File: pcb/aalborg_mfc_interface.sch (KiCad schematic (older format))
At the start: 27 parts, among them J1 DB15FV, J2 DB15FV, J3 DB15FV, P1 PWR_JACK_2.5x5.5, P2 HEADER_01X03, P3 HEADER_01X03, P4 HEADER_01X03, P5 HEADER_01X03, SW1 SPST_SERIES_M, U1 MAX6817

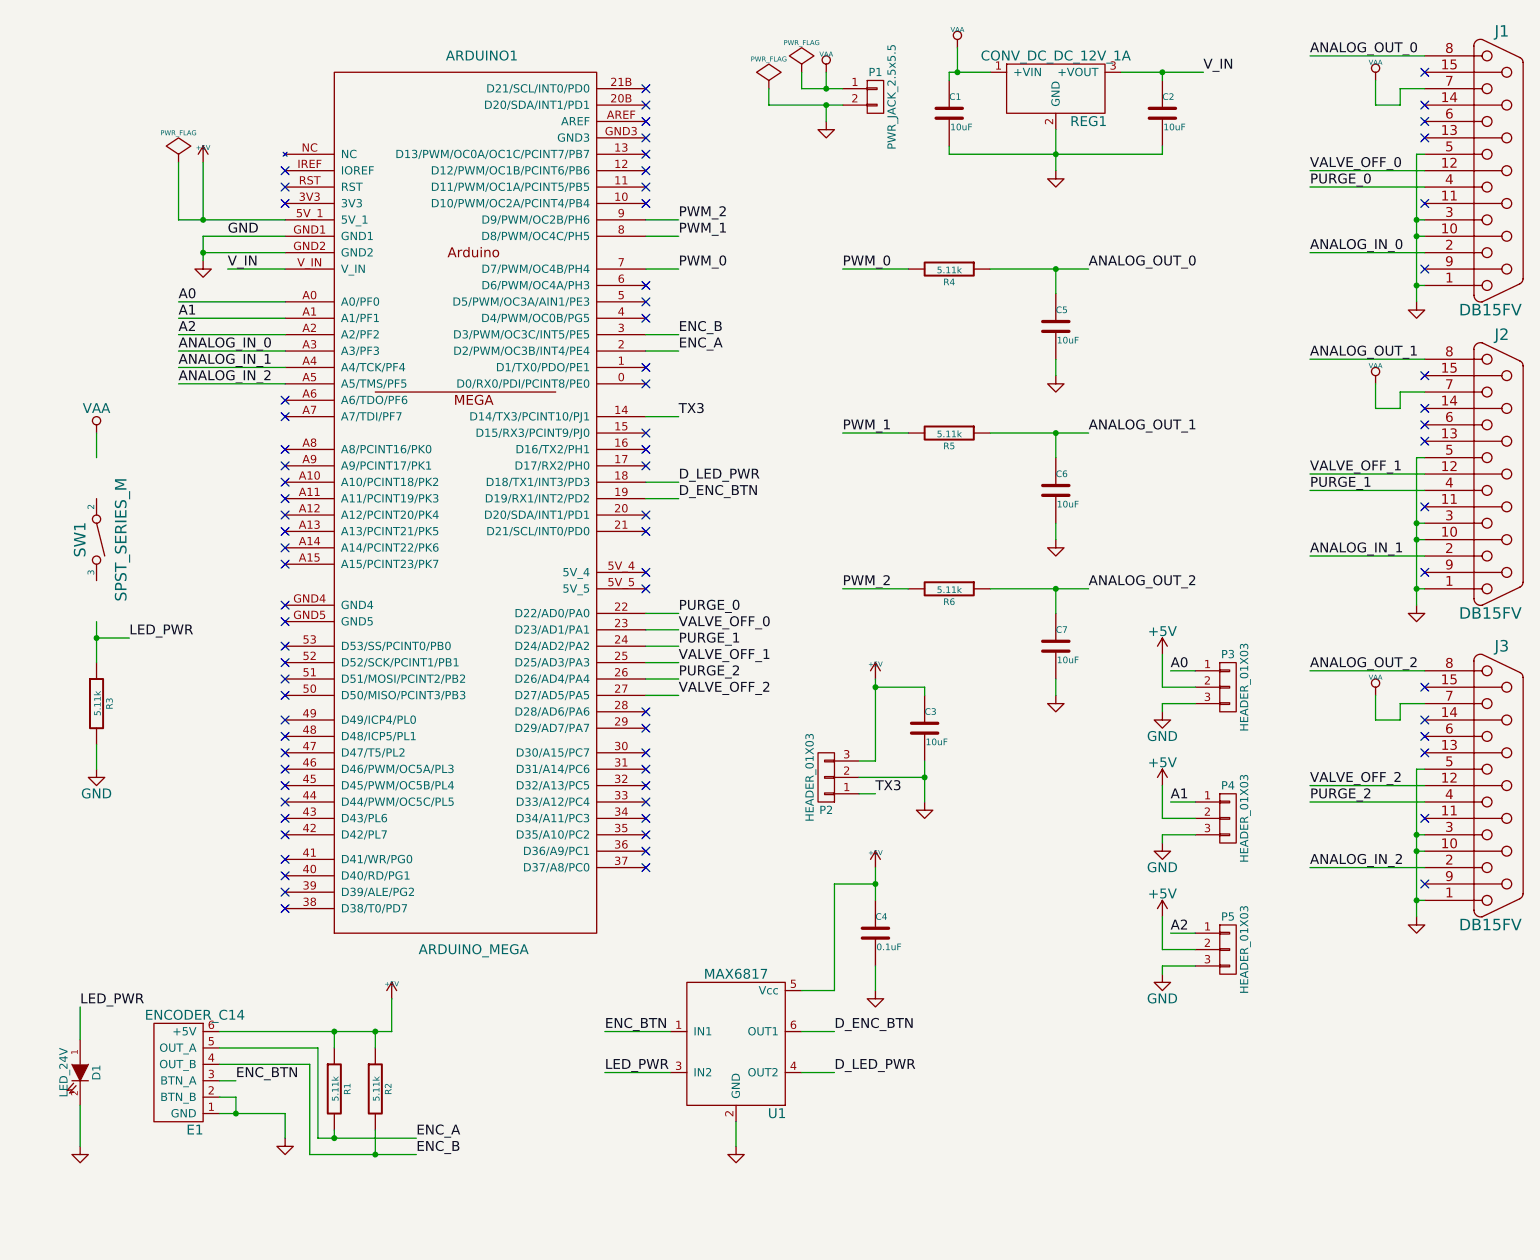
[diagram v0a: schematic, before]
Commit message: Progress on pcb 1.1 design and firmware 1.0.
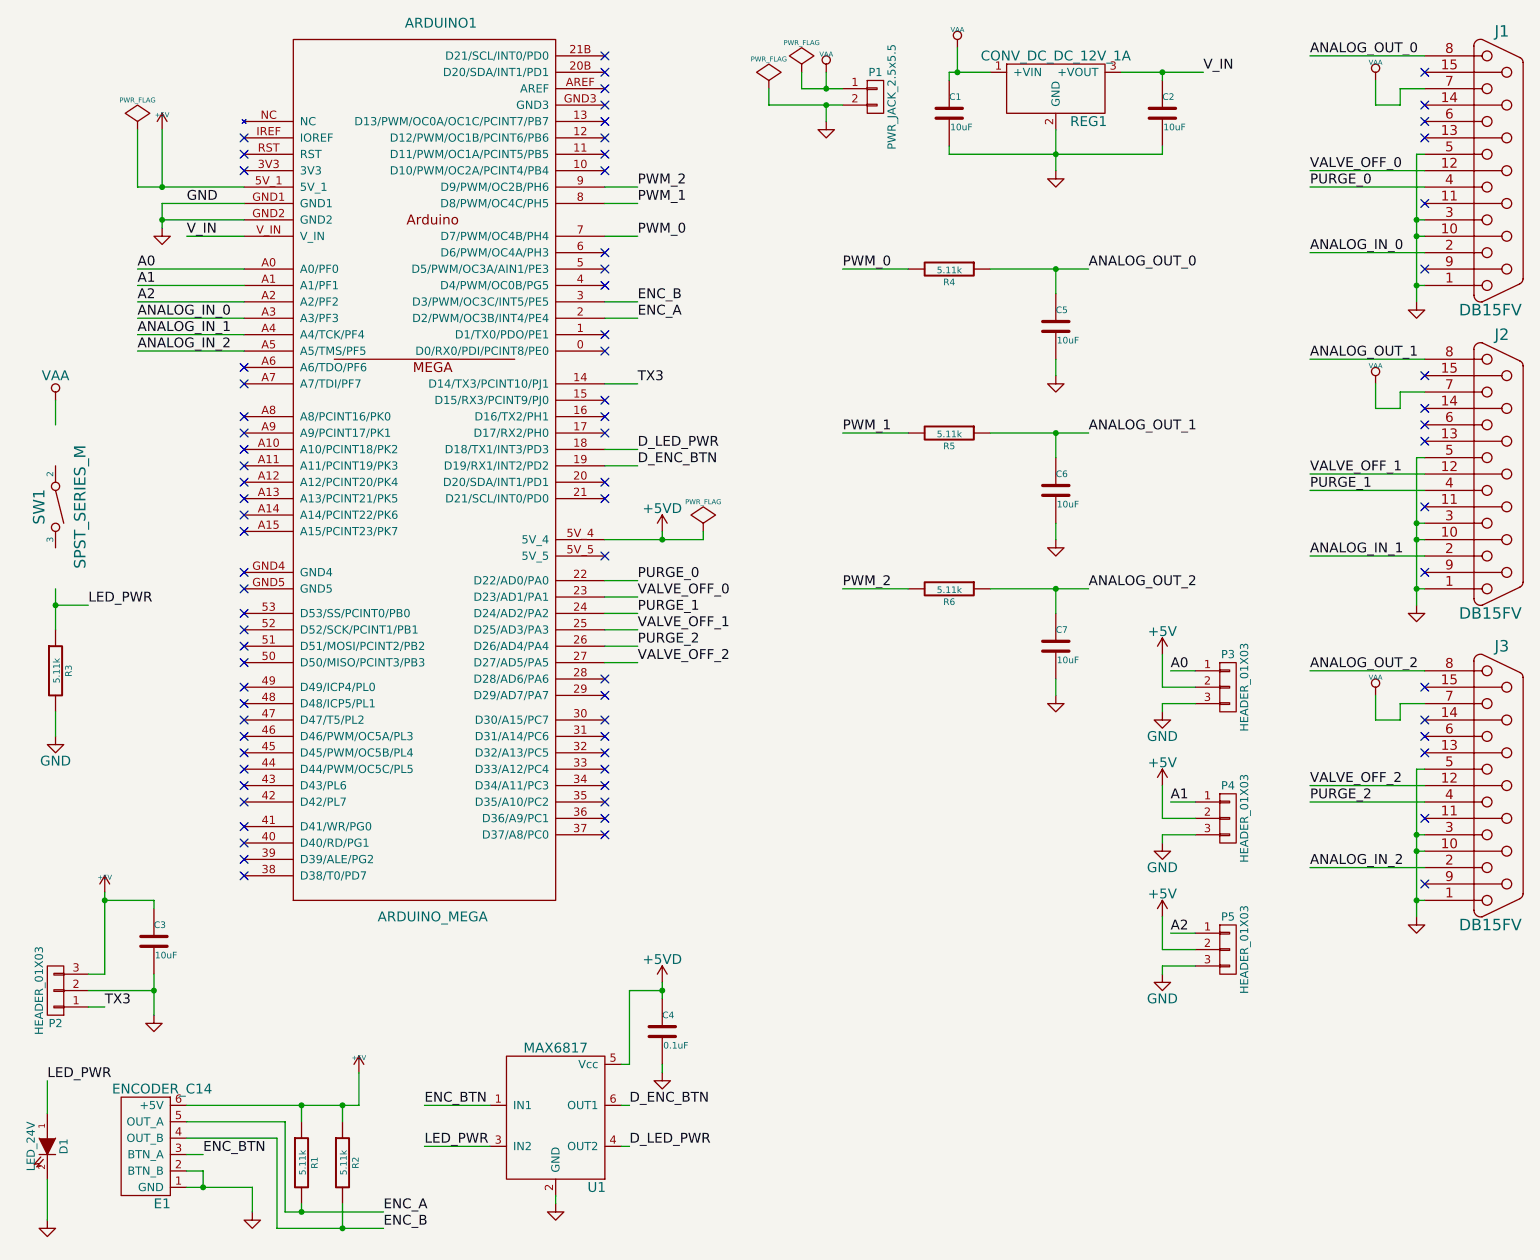
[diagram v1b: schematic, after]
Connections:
- net +5V: no longer C4.1, U1.5 (Vcc)
- net +5VD: now reaches ARDUINO1.5V_4
- net +5VD: now also C4.1, U1.5 (Vcc)
- no-connect marks 79 -> 78
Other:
- moved on the sheet: ARDUINO1, C3, C4, D1, E1, P2, R1, R2, R3, SW1, U1

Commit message: Progress towards pcb v1.1.
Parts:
- removed P3, P4, P5: HEADER_01X03, aalborg_mfc_interface:Header_Shrouded_3_Pin, symbol HEADER_01X03
- added C5: 0.1uF, aalborg_mfc_interface:SM1210, symbol 0.1uF
- added P3, P4, P5: HEADER_01X03_SHR, aalborg_mfc_interface:Header_Shrouded_3_Pin, symbol HEADER_01X03_SHR
- added S1: HEADER_01X02, aalborg_mfc_interface:Header_Shrouded_2_Pin, symbol HEADER_01X02
- added SW2: KT_SWITCH, aalborg_mfc_interface:KT_SWITCH, symbol KT_SWITCH
- added U2: MAX6817, aalborg_mfc_interface:MAX6817, symbol MAX6817
- P2: footprint aalborg_mfc_interface:Header_Shrouded_3_Pin -> aalborg_mfc_interface:Header_3_Pin
- renumbered C5 to C6, C6 to C7, C7 to C8
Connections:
- net +5V: now also P3.2 (P2), P4.2 (P2), P5.2 (P2)
- net +5VD: now also C5.1, U2.5 (Vcc)
- net A0: now also P3.1 (P1)
- net A1: now also P4.1 (P1)
- net A2: now also P5.1 (P1)
- net GND: now also C5.2, P3.3 (P3), P4.3 (P3), P5.3 (P3), S1.2 (P2), SW2.3, U2.2 (GND)
- net LED_PWR: now also SW1.3
- net VAA: now also SW1.2
- net D_D20: now reaches ARDUINO1.20 (D20/SDA/INT1/PD1)
- net D_D20: now also U2.4 (OUT2)
- net D_D21: now reaches ARDUINO1.21 (D21/SCL/INT0/PD0)
- net D_D21: now also U2.6 (OUT1)
- new net D20: S1.1 (P1), U2.3 (IN2)
- new net D21: SW2.2, U2.1 (IN1)
- no-connect marks 78 -> 76
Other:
- moved on the sheet: C4, D1, E1, R1, R2, U1

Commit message: Minor changes to names.
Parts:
- removed S1: HEADER_01X02, aalborg_mfc_interface:Header_Shrouded_2_Pin, symbol HEADER_01X02
- added S1: HEADER_01X02_SHR, aalborg_mfc_interface:Header_Shrouded_2_Pin, symbol HEADER_01X02_SHR
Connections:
- net GND: now also S1.2 (P2)
- net D20 renamed IN
- net IN: now also S1.1 (P1)
- net D21 renamed BTN
- net D_D20 renamed D_IN
- net D_D21 renamed D_BTN
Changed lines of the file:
@@
 	1200 1200 1200 1550
 Wire Wire Line
-	1200 1550 1850 1550
+	1200 1550 1350 1550
+Wire Wire Line
+	1350 1550 1850 1550
 Wire Wire Line
 	1350 1200 1350 1550
@@
 	1850 1650 1350 1650
 Wire Wire Line
-	1350 1650 1350 1800
+	1350 1650 1350 1750
+Wire Wire Line
+	1350 1750 1350 1800
 Wire Wire Line
 	1850 1750 1350 1750
@@
 $EndComp
 Wire Wire Line
-	5250 950  5500 950
+	5250 950  5400 950
+Wire Wire Line
+	5400 950  5500 950
 Wire Wire Line
 	5250 950  5250 850
@@
 Connection ~ 5400 950
 Wire Wire Line
-	5050 1050 5500 1050
+	5050 1050 5400 1050
+Wire Wire Line
+	5400 1050 5500 1050
 Wire Wire Line
 	5050 1050 5050 950
@@
 $EndComp
 Wire Wire Line
-	1300 6350 1300 6600
+	1300 6350 1300 6450
+Wire Wire Line
+	1300 6450 1300 6600
 Wire Wire Line
 	900  6450 1300 6450
@@
 	1300 5900 1000 5900
 Wire Wire Line
-	1000 5850 1000 6350
+	1000 5850 1000 5900
+Wire Wire Line
+	1000 5900 1000 6350
 Wire Wire Line
 	1000 6350 900  6350
@@
 $EndComp
 Wire Wire Line
-	6800 1200 6800 1450
+	6800 1200 6800 1350
+Wire Wire Line
+	6800 1350 6800 1450
 Wire Wire Line
 	6150 1300 6150 1350
 Wire Wire Line
-	6150 1350 7450 1350
+	6150 1350 6800 1350
+Wire Wire Line
+	6800 1350 7450 1350
 Connection ~ 6800 1350
 Wire Wire Line
@@
 	6150 900  6150 850
 Wire Wire Line
-	6150 850  6400 850
-Wire Wire Line
-	7200 850  7700 850
+	6150 850  6200 850
+Wire Wire Line
+	6200 850  6400 850
+Wire Wire Line
+	7200 850  7450 850
+Wire Wire Line
+	7450 850  7700 850
 Wire Wire Line
 	7450 900  7450 850
@@
 $EndComp
 Wire Wire Line
-	950  7550 1350 7550
+	950  7550 1050 7550
+Wire Wire Line
+	1050 7550 1350 7550
 Wire Wire Line
 	1350 7550 1350 7700
@@
 $EndComp
 Wire Wire Line
-	950  7050 2000 7050
+	950  7050 1650 7050
+Wire Wire Line
+	1650 7050 1900 7050
+Wire Wire Line
+	1900 7050 2000 7050
 Wire Wire Line
 	2000 7050 2000 6850
@@
 	1550 7150 1550 7700
 Wire Wire Line
-	1550 7700 1950 7700
+	1550 7700 1650 7700
+Wire Wire Line
+	1650 7700 1950 7700
 Wire Wire Line
 	950  7250 1500 7250
@@
 	1500 7250 1500 7800
 Wire Wire Line
-	1500 7800 1950 7800
+	1500 7800 1900 7800
+Wire Wire Line
+	1900 7800 1950 7800
 Text Label 1050 7350 0    60   ~ 0
 ENC_BTN
@@
 	3750 7000 3750 7050
 Wire Wire Line
-	3750 6500 3750 6600
+	3750 6500 3750 6550
+Wire Wire Line
+	3750 6550 3750 6600
 Wire Wire Line
 	4050 3250 4250 3250
@@
 	9050 1350 9000 1350
 Wire Wire Line
-	9000 1350 9000 2250
+	9000 1350 9000 1750
+Wire Wire Line
+	9000 1750 9000 1850
+Wire Wire Line
+	9000 1850 9000 2150
+Wire Wire Line
+	9000 2150 9000 2250
 Wire Wire Line
 	9050 2150 9000 2150
@@
 	6800 2600 6800 2700
 Wire Wire Line
-	6400 2050 7000 2050
+	6400 2050 6800 2050
+Wire Wire Line
+	6800 2050 7000 2050
 Wire Wire Line
 	6800 2200 6800 2050
@@
 	6800 3600 6800 3700
 Wire Wire Line
-	6400 3050 7000 3050
+	6400 3050 6800 3050
+Wire Wire Line
+	6800 3050 7000 3050
 Wire Wire Line
 	6800 3200 6800 3050
@@
 	9050 3200 9000 3200
 Wire Wire Line
-	9000 3200 9000 4100
+	9000 3200 9000 3600
+Wire Wire Line
+	9000 3600 9000 3700
+Wire Wire Line
+	9000 3700 9000 4000
+Wire Wire Line
+	9000 4000 9000 4100
 Wire Wire Line
 	9050 4000 9000 4000
@@
 $EndComp
 Wire Wire Line
-	700  4000 700  4250
+	700  4000 700  4100
+Wire Wire Line
+	700  4100 700  4250
 Wire Wire Line
 	700  4750 700  4900
@@
 	9050 5100 9000 5100
 Wire Wire Line
-	9000 5100 9000 6000
+	9000 5100 9000 5500
+Wire Wire Line
+	9000 5500 9000 5600
+Wire Wire Line
+	9000 5600 9000 5900
+Wire Wire Line
+	9000 5900 9000 6000
 Wire Wire Line
 	9050 5900 9000 5900
@@
 	6800 4550 6800 4650
 Wire Wire Line
-	6400 4000 7000 4000
+	6400 4000 6800 4000
+Wire Wire Line
+	6800 4000 7000 4000
 Wire Wire Line
 	6800 4150 6800 4000
@@
 $EndComp
 Wire Wire Line
-	4050 3700 4650 3700
+	4050 3700 4400 3700
+Wire Wire Line
+	4400 3700 4650 3700
 Wire Wire Line
 	4400 3700 4400 3650
@@
 	4550 7250 4150 7250
 Text Label 4150 7250 0    60   ~ 0
-D21
+BTN
 Wire Wire Line
 	5350 7250 5400 7250
 Text Label 5400 7250 0    60   ~ 0
-D_D21
+D_BTN
 $Comp
 L GND #PWR037
@@
 	5600 7000 5600 7050
 Wire Wire Line
-	5600 6500 5600 6600
+	5600 6500 5600 6550
+Wire Wire Line
+	5600 6550 5600 6600
 $Comp
 L 0.1uF C5
@@
 	4550 7500 4150 7500
 Text Label 4150 7500 0    60   ~ 0
-D20
+IN
 Wire Wire Line
 	5350 7500 5400 7500
 Text Label 5400 7500 0    60   ~ 0
-D_D20
+D_IN
 $Comp
 L +5VD #PWR039
@@
 	5400 6550 5600 6550
 Connection ~ 5600 6550
-$Comp
-L HEADER_01X02 S1
-U 1 1 54B95C4E
-P 4650 6500
-F 0 "S1" H 4650 6650 50  0000 C CNN
-F 1 "HEADER_01X02" V 4750 6500 50  0000 C CNN
-F 2 "aalborg_mfc_interface:Header_Shrouded_2_Pin" H 4550 6550 60  0001 C CNN
-F 3 "" H 4650 6500 60  0000 C CNN
-F 4 "digikey" H 4750 6750 60  0001 C CNN "Vendor"
-F 5 "WM4800-ND" H 4850 6850 60  0001 C CNN "PartNumber"
-F 6 "CONN HEADER 2POS .100 VERT GOLD" H 4950 6950 60  0001 C CNN "Description"
-	1    4650 6500
-	1    0    0    -1
-$EndComp
-Wire Wire Line
-	4450 6450 4200 6450
-Text Label 4200 6450 0    60   ~ 0
-D20
+Wire Wire Line
+	4400 6450 4300 6450
+Text Label 4300 6450 0    60   ~ 0
+IN
 $Comp
 L GND #PWR040
 U 1 1 54B961A4
-P 4350 6600
-F 0 "#PWR040" H 4350 6350 60  0001 C CNN
-F 1 "GND" H 4350 6450 60  0000 C CNN
-F 2 "" H 4350 6600 60  0000 C CNN
-F 3 "" H 4350 6600 60  0000 C CNN
-	1    4350 6600
-	1    0    0    -1
-$EndComp
-Wire Wire Line
-	4350 6600 4350 6550
-Wire Wire Line
-	4350 6550 4450 6550
+P 4300 6600
+F 0 "#PWR040" H 4300 6350 60  0001 C CNN
+F 1 "GND" H 4300 6450 60  0000 C CNN
+F 2 "" H 4300 6600 60  0000 C CNN
+F 3 "" H 4300 6600 60  0000 C CNN
+	1    4300 6600
+	1    0    0    -1
+$EndComp
+Wire Wire Line
+	4300 6600 4300 6550
+Wire Wire Line
+	4300 6550 4400 6550
 $Comp
 L SPST_SERIES_M SW1
@@
 	4050 3450 4250 3450
 Text Label 4250 3450 0    60   ~ 0
-D_D21
+D_BTN
 Text Label 4250 3350 0    60   ~ 0
-D_D20
+D_IN
 $Comp
 L GND #PWR041
@@
 	5950 7200 5950 7050
 Text Label 5950 7050 0    60   ~ 0
-D21
+BTN
 $Comp
 L KT_SWITCH SW2
@@
 	-1   0    0    1
 $EndComp
+$Comp
+L HEADER_01X02_SHR S1
+U 1 1 54BEC0BB
+P 4600 6500
+F 0 "S1" H 4600 6650 50  0000 C CNN
+F 1 "HEADER_01X02_SHR" V 4700 6500 50  0000 C CNN
+F 2 "aalborg_mfc_interface:Header_Shrouded_2_Pin" H 4500 6550 60  0001 C CNN
+F 3 "" H 4600 6500 60  0000 C CNN
+F 4 "digikey" H 4700 6750 60  0001 C CNN "Vendor"
+F 5 "WM4800-ND" H 4800 6850 60  0001 C CNN "PartNumber"
+F 6 "CONN HEADER 2POS .100 VERT GOLD" H 4900 6950 60  0001 C CNN "Description"
+	1    4600 6500
+	1    0    0    -1
+$EndComp
 $EndSCHEMATC
